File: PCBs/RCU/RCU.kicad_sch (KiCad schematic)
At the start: 0 parts

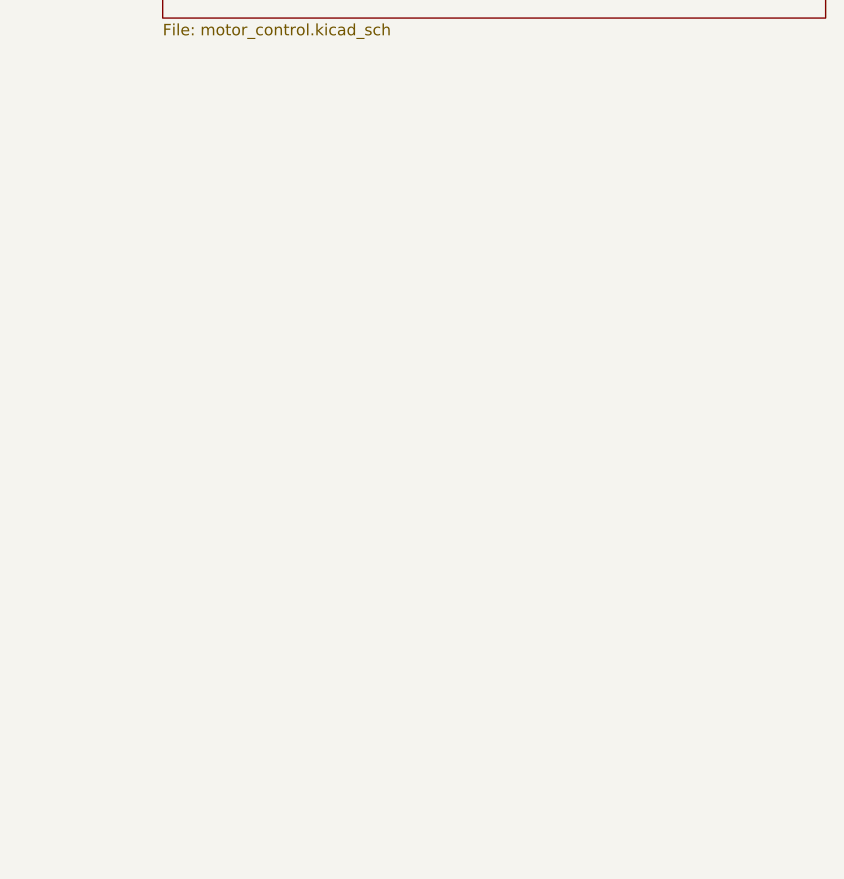
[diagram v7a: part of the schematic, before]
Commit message: Added ADC circuit for sensing motor currents
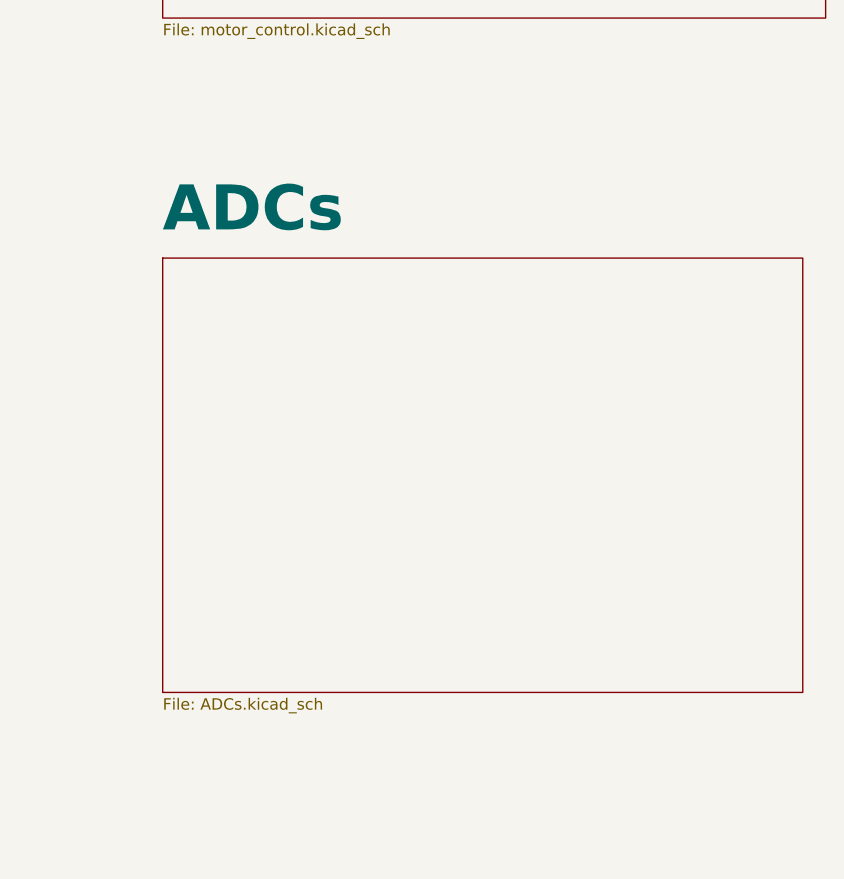
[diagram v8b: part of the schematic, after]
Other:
- added sheet ADCs (ADCs.kicad_sch)
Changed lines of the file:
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@@
+    )
+  )
+  (sheet (at 139.7 114.3) (size 71.12 48.26) (fields_autoplaced)
+    (stroke (width 0.1524) (type solid) (color 0 0 0 0))
+    (fill (color 0 0 0 0.0000))
+    (property "Sheet name" "ADCs" (id 0) (at 139.7 111.7234 0)
+      (effects (font (size 5 5) bold) (justify left bottom))
+    )
+    (property "Sheet file" "ADCs.kicad_sch" (id 1) (at 139.7 163.1446 0)
+      (effects (font (size 1.27 1.27)) (justify left top))
     )
   )
@@
     (path "/2537d888-fd78-4661-a6de-7d85959a9016" (page "3"))
     (path "/6678d44b-178f-4b7c-833f-18a4e680f820" (page "4"))
+    (path "/d249f484-be7b-4fe1-aa74-bf5965c8a2c2" (page "5"))
   )
   (symbol_instances
@@
       (reference "#PWR?") (unit 1) (value "GND") (footprint "")
     )
+    (path "/d249f484-be7b-4fe1-aa74-bf5965c8a2c2/05cc657e-9df0-430f-b6fb-3f6695e7a346"
+      (reference "#PWR?") (unit 1) (value "GND") (footprint "")
+    )
     (path "/6678d44b-178f-4b7c-833f-18a4e680f820/0b164fde-4117-4f4b-b33c-90ef4e14a2d7"
       (reference "#PWR?") (unit 1) (value "GND") (footprint "")
@@
       (reference "#PWR?") (unit 1) (value "GND") (footprint "")
     )
+    (path "/d249f484-be7b-4fe1-aa74-bf5965c8a2c2/256b3d94-ff8e-4336-82c0-0e2eaced389f"
+      (reference "#PWR?") (unit 1) (value "+3.3VA") (footprint "")
+    )
     (path "/6678d44b-178f-4b7c-833f-18a4e680f820/2f1ef7f6-3da7-40c6-9050-7587459efbf1"
       (reference "#PWR?") (unit 1) (value "+3.3V") (footprint "")
@@
       (reference "#PWR?") (unit 1) (value "GND") (footprint "")
     )
+    (path "/d249f484-be7b-4fe1-aa74-bf5965c8a2c2/4232db08-69fa-4e5c-a833-0fe5b8e1b1be"
+      (reference "#PWR?") (unit 1) (value "GND") (footprint "")
+    )
     (path "/2537d888-fd78-4661-a6de-7d85959a9016/43f244d5-2197-4bfe-a0c5-e1fd26776c80"
+      (reference "#PWR?") (unit 1) (value "GND") (footprint "")
+    )
+    (path "/d249f484-be7b-4fe1-aa74-bf5965c8a2c2/4592a8d3-bc3f-48ff-aad4-bfd43da1ce84"
+      (reference "#PWR?") (unit 1) (value "GND") (footprint "")
+    )
+    (path "/d249f484-be7b-4fe1-aa74-bf5965c8a2c2/46564e5e-3ce8-4853-9c5a-21f8764785af"
       (reference "#PWR?") (unit 1) (value "GND") (footprint "")
     )
@@
       (reference "#PWR?") (unit 1) (value "+3.3V") (footprint "")
     )
-    (path "/2537d888-fd78-4661-a6de-7d85959a9016/517a3688-e403-4013-ab18-7e5bef52e7d0"
-      (reference "#PWR?") (unit 1) (value "GND") (footprint "")
+    (path "/d249f484-be7b-4fe1-aa74-bf5965c8a2c2/52a5209d-bd4b-4508-82e2-8246371d86e8"
+      (reference "#PWR?") (unit 1) (value "+3.3VA") (footprint "")
     )
     (path "/6678d44b-178f-4b7c-833f-18a4e680f820/5469af30-69da-464c-a352-5a7564a6c776"
@@
       (reference "#PWR?") (unit 1) (value "VCC") (footprint "")
     )
-    (path "/2537d888-fd78-4661-a6de-7d85959a9016/63b4d81d-543e-43bf-8722-61fa09ade79d"
-      (reference "#PWR?") (unit 1) (value "+3.3V") (footprint "")
+    (path "/d249f484-be7b-4fe1-aa74-bf5965c8a2c2/63a3a084-e152-404f-b7d2-df6cefc0dcdb"
+      (reference "#PWR?") (unit 1) (value "+3.3VA") (footprint "")
     )
     (path "/2537d888-fd78-4661-a6de-7d85959a9016/725f7d01-38c4-4798-a9e5-547e4c0fa8b1"
@@
       (reference "#PWR?") (unit 1) (value "GND") (footprint "")
     )
-    (path "/2537d888-fd78-4661-a6de-7d85959a9016/7e00a6a0-514f-4c83-b28e-ae734fa499f8"
-      (reference "#PWR?") (unit 1) (value "GND") (footprint "")
-    )
     (path "/c46a482e-bfa4-4ed5-a49f-3179709c39a1/8f435151-c909-4cdf-a7f9-67c1f7b1e16c"
       (reference "#PWR?") (unit 1) (value "GND") (footprint "")
@@
       (reference "#PWR?") (unit 1) (value "GND") (footprint "")
     )
+    (path "/d249f484-be7b-4fe1-aa74-bf5965c8a2c2/a68b708e-eb5e-4c40-8ed1-0ffd8f816d22"
+      (reference "#PWR?") (unit 1) (value "GND") (footprint "")
+    )
+    (path "/d249f484-be7b-4fe1-aa74-bf5965c8a2c2/a8c64bdd-4bad-4dfe-9947-e954dc30b04b"
+      (reference "#PWR?") (unit 1) (value "+3.3VA") (footprint "")
+    )
     (path "/2537d888-fd78-4661-a6de-7d85959a9016/ac6c9020-18df-42e7-9dbc-fa0e350749f6"
       (reference "#PWR?") (unit 1) (value "GND") (footprint "")
@@
       (reference "#PWR?") (unit 1) (value "GND") (footprint "")
     )
+    (path "/d249f484-be7b-4fe1-aa74-bf5965c8a2c2/bdb2c66b-7004-4fd2-8636-62b5fe073af1"
+      (reference "#PWR?") (unit 1) (value "GND") (footprint "")
+    )
     (path "/c46a482e-bfa4-4ed5-a49f-3179709c39a1/c614826f-045e-4277-8c63-7b6a187f6ea8"
       (reference "#PWR?") (unit 1) (value "+3.3V") (footprint "")
@@
     )
     (path "/2537d888-fd78-4661-a6de-7d85959a9016/e8ce0d43-f3a4-442a-830b-4bbd90cbb70e"
-      (reference "#PWR?") (unit 1) (value "+3.3V") (footprint "")
-    )
-    (path "/2537d888-fd78-4661-a6de-7d85959a9016/ee910aec-70e9-4f16-96e4-d98b11ee7154"
       (reference "#PWR?") (unit 1) (value "+3.3V") (footprint "")
     )
@@
       (reference "#PWR?") (unit 1) (value "GND") (footprint "")
     )
-    (path "/2537d888-fd78-4661-a6de-7d85959a9016/15392497-5edb-4e94-86ed-ca89e5c94002"
-      (reference "C") (unit 1) (value "10u") (footprint "")
-    )
     (path "/2537d888-fd78-4661-a6de-7d85959a9016/ae4b09e3-6502-4f4e-a59d-c4c57af5b5fa"
       (reference "C") (unit 1) (value "22nF") (footprint "")
@@
       (reference "C?") (unit 1) (value "1uF") (footprint "")
     )
+    (path "/d249f484-be7b-4fe1-aa74-bf5965c8a2c2/11371c3e-7911-4cfd-bc27-6ee985534c48"
+      (reference "C?") (unit 1) (value "0.1uF") (footprint "")
+    )
     (path "/c46a482e-bfa4-4ed5-a49f-3179709c39a1/14fed118-9356-4bd7-9725-712b0ee562db"
       (reference "C?") (unit 1) (value "C") (footprint "")
     )
+    (path "/d249f484-be7b-4fe1-aa74-bf5965c8a2c2/2a2a439a-9cf7-4ac8-821a-ce78a1a8d23d"
+      (reference "C?") (unit 1) (value "10u") (footprint "")
+    )
     (path "/2537d888-fd78-4661-a6de-7d85959a9016/3bd3a7ea-acd6-4a25-b3c3-da625d06d885"
       (reference "C?") (unit 1) (value "0.1uF") (footprint "")
     )
-    (path "/2537d888-fd78-4661-a6de-7d85959a9016/5a94a684-6865-4241-b43e-45e356886b3d"
-      (reference "C?") (unit 1) (value "10u") (footprint "")
-    )
-    (path "/2537d888-fd78-4661-a6de-7d85959a9016/5f9510b7-2331-4e61-b678-ec769917fa44"
-      (reference "C?") (unit 1) (value "0.1uF") (footprint "")
-    )
-    (path "/2537d888-fd78-4661-a6de-7d85959a9016/7b6e356f-c3d9-45e5-b60a-7ae86ba3c876"
-      (reference "C?") (unit 1) (value "0.1uF") (footprint "")
+    (path "/d249f484-be7b-4fe1-aa74-bf5965c8a2c2/72c3c7a5-a9a8-44bf-bd10-9a3702fd0341"
+      (reference "C?") (unit 1) (value "0.1u") (footprint "")
     )
     (path "/c46a482e-bfa4-4ed5-a49f-3179709c39a1/87164916-93ae-4140-86aa-59470124ec1a"
@@
     )
     (path "/6678d44b-178f-4b7c-833f-18a4e680f820/8c718c35-c183-4a0e-890d-6e260578dfc8"
-      (reference "C?") (unit 1) (value "100nF") (footprint "")
+      (reference "C?") (unit 1) (value "0.1uF") (footprint "")
     )
     (path "/2537d888-fd78-4661-a6de-7d85959a9016/a00878f2-8d2f-4913-a444-67c62f967c26"
       (reference "C?") (unit 1) (value "22nF") (footprint "")
     )
+    (path "/d249f484-be7b-4fe1-aa74-bf5965c8a2c2/aadfd5c4-5be8-4116-8d65-8da20cd7b1c3"
+      (reference "C?") (unit 1) (value "10u") (footprint "")
+    )
+    (path "/d249f484-be7b-4fe1-aa74-bf5965c8a2c2/b2cbebee-aba9-4c2f-98ce-5dbd7f674d41"
+      (reference "C?") (unit 1) (value "0.1uF") (footprint "")
+    )
     (path "/6678d44b-178f-4b7c-833f-18a4e680f820/dc1c28c6-7dcc-46b4-b1a4-fd631cfd2412"
       (reference "C?") (unit 1) (value "100nF") (footprint "")
@@
       (reference "C?") (unit 1) (value "0.1uF") (footprint "")
     )
+    (path "/d249f484-be7b-4fe1-aa74-bf5965c8a2c2/fe7573c9-527b-483b-894d-fb42e352e452"
+      (reference "C?") (unit 1) (value "0.1u") (footprint "")
+    )
     (path "/2537d888-fd78-4661-a6de-7d85959a9016/5e3aabe0-81fe-4111-bf58-7d47c2f8f111"
       (reference "J?") (unit 1) (value "Screw_Terminal_01x02") (footprint "")
@@
       (reference "R?") (unit 1) (value "10k") (footprint "")
     )
+    (path "/d249f484-be7b-4fe1-aa74-bf5965c8a2c2/28d0a302-e781-40e8-9151-8928483ba027"
+      (reference "R?") (unit 1) (value "1.6k") (footprint "")
+    )
+    (path "/d249f484-be7b-4fe1-aa74-bf5965c8a2c2/327e245b-e617-4067-8f13-44101e46f37d"
+      (reference "R?") (unit 1) (value "1.6k") (footprint "")
+    )
     (path "/6678d44b-178f-4b7c-833f-18a4e680f820/62ebd1cf-5b9b-4bab-92c2-efb41e0af239"
       (reference "R?") (unit 1) (value "10k") (footprint "")
@@
       (reference "U?") (unit 1) (value "DRV8876") (footprint "")
     )
+    (path "/d249f484-be7b-4fe1-aa74-bf5965c8a2c2/3865ebee-a15c-453b-bf9a-2288810c0237"
+      (reference "U?") (unit 1) (value "TLV2371DBV") (footprint "Package_TO_SOT_SMD:SOT-23-5")
+    )
     (path "/6678d44b-178f-4b7c-833f-18a4e680f820/455511d5-40a2-4651-ab9c-da84f8d67b49"
       (reference "U?") (unit 1) (value "SHT30-DIS") (footprint "Sensor_Humidity:Sensirion_DFN-8-1EP_2.5x2.5mm_P0.5mm_EP1.1x1.7mm")
     )
-    (path "/2537d888-fd78-4661-a6de-7d85959a9016/49b6ef3c-8160-4199-a4dc-383aaa761e83"
-      (reference "U?") (unit 1) (value "MCP3021A5T-E/OT") (footprint "")
-    )
-    (path "/2537d888-fd78-4661-a6de-7d85959a9016/84e0121f-799e-46d9-9628-754dbbfbafc9"
+    (path "/d249f484-be7b-4fe1-aa74-bf5965c8a2c2/515bebc9-1ab2-413f-b2a9-61ad67eff9cf"
+      (reference "U?") (unit 1) (value "TLV2371DBV") (footprint "Package_TO_SOT_SMD:SOT-23-5")
+    )
+    (path "/d249f484-be7b-4fe1-aa74-bf5965c8a2c2/7feb8a1b-3f2a-4be2-82b2-706f9df82096"
       (reference "U?") (unit 1) (value "MCP3021A5T-E/OT") (footprint "")
     )
@@
       (reference "U?") (unit 1) (value "LSM6DS3") (footprint "Package_LGA:LGA-14_3x2.5mm_P0.5mm_LayoutBorder3x4y")
     )
+    (path "/d249f484-be7b-4fe1-aa74-bf5965c8a2c2/ec7d9904-e541-4a51-83e0-13ec043411de"
+      (reference "U?") (unit 1) (value "MCP3021A5T-E/OT") (footprint "")
+    )
     (path "/c46a482e-bfa4-4ed5-a49f-3179709c39a1/65321985-657f-4e17-a0a5-f2f7935eae83"
